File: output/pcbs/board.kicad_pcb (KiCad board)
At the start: 2 copper layers, 122.3 x 101.1 mm, 48 parts, among them J1 Jumper, J2 Jumper

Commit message: finish up
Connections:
- MCU1 pad 25: B- -> Bminus
- MCU2 pad 25: B- -> Bminus
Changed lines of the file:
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@@
 (net 39 "P8")
 (net 40 "P9")
-(net 41 "B+")
-(net 42 "B-")
+(net 41 "Bplus")
+(net 42 "Bminus")
 (net 43 "Braw")
-(net 44 "Bminus")
-(net 45 "Bplus")
   (net_class Default "This is the default net class."
     (clearance 0.2)
@@
 (add_net "P8")
 (add_net "P9")
-(add_net "B+")
-(add_net "B-")
-(add_net "Braw")
-(add_net "Bminus")
-(add_net "Bplus")
   )
   (net_class Power "This is the power net class."
@@
 (add_net "GND")
 (add_net "VCC")
+(add_net "Bplus")
+(add_net "Bminus")
+(add_net "Braw")
   )
       (module PG1350 (layer F.Cu)
@@
           (fp_text user "B+" (at -16.51 -4.8 360) (layer B.SilkS) (effects (font (size 0.8 0.8) (thickness 0.15)) (justify mirror)))
           (fp_text user "B-" (at -16.51 4.8 360) (layer B.SilkS) (effects (font (size 0.8 0.8) (thickness 0.15)) (justify mirror)))
-          (pad 25 thru_hole roundrect (at -16.51 -7.62 0) (size 1.5 1.5) (drill 1.0922) (layers *.Cu *.SilkS *.Mask) (roundrect_rratio 0.25) (net 41 "B+"))
-          (pad 25 thru_hole roundrect (at -16.51 7.62 0) (size 1.5 1.5) (drill 1.0922) (layers *.Cu *.SilkS *.Mask) (roundrect_rratio 0.25) (net 42 "B-"))
+          (pad 25 thru_hole roundrect (at -16.51 -7.62 0) (size 1.5 1.5) (drill 1.0922) (layers *.Cu *.SilkS *.Mask) (roundrect_rratio 0.25) (net 41 "Bplus"))
+          (pad 25 thru_hole roundrect (at -16.51 7.62 0) (size 1.5 1.5) (drill 1.0922) (layers *.Cu *.SilkS *.Mask) (roundrect_rratio 0.25) (net 42 "Bminus"))
         )
         (module ProMicro (layer F.Cu)
@@
           (fp_text user "B+" (at -16.51 4.8 360) (layer F.SilkS) (effects (font (size 0.8 0.8) (thickness 0.15)) ))
           (fp_text user "B-" (at -16.51 -4.8 360) (layer F.SilkS) (effects (font (size 0.8 0.8) (thickness 0.15)) ))
-          (pad 25 thru_hole roundrect (at -16.51 7.62 0) (size 1.5 1.5) (drill 1.0922) (layers *.Cu *.SilkS *.Mask) (roundrect_rratio 0.25) (net 41 "B+"))
-          (pad 25 thru_hole roundrect (at -16.51 -7.62 0) (size 1.5 1.5) (drill 1.0922) (layers *.Cu *.SilkS *.Mask) (roundrect_rratio 0.25) (net 42 "B-"))
+          (pad 25 thru_hole roundrect (at -16.51 7.62 0) (size 1.5 1.5) (drill 1.0922) (layers *.Cu *.SilkS *.Mask) (roundrect_rratio 0.25) (net 41 "Bplus"))
+          (pad 25 thru_hole roundrect (at -16.51 -7.62 0) (size 1.5 1.5) (drill 1.0922) (layers *.Cu *.SilkS *.Mask) (roundrect_rratio 0.25) (net 42 "Bminus"))
         )
         (module SMDPad (layer F.Cu)
@@
             (fp_text reference "PAD2" (at 0 0) (layer F.SilkS) hide (effects (font (size 1.27 1.27) (thickness 0.15))))
             (fp_text value "" (at 0 0) (layer F.SilkS) hide (effects (font (size 1.27 1.27) (thickness 0.15))))
-            (pad 1 smd rect (at 0 0 0) (size 1.5 1.5) (layers F.Cu F.Paste F.Mask) (net 44 "Bminus"))
+            (pad 1 smd rect (at 0 0 0) (size 1.5 1.5) (layers F.Cu F.Paste F.Mask) (net 42 "Bminus"))
 (fp_text user B- (at -2.25 0 0) (layer F.SilkS) (effects (font (size 0.8 0.8) (thickness 0.15)) ))
-            (pad 1 smd rect (at 0 0 0) (size 1.5 1.5) (layers B.Cu B.Paste B.Mask) (net 44 "Bminus"))
+            (pad 1 smd rect (at 0 0 0) (size 1.5 1.5) (layers B.Cu B.Paste B.Mask) (net 42 "Bminus"))
 (fp_text user B- (at -2.25 0 0) (layer B.SilkS) (effects (font (size 0.8 0.8) (thickness 0.15)) (justify mirror)))
         )
@@
         (clearance 0.1905) (net 43 "Braw"))
         (pad 2 smd rect (at 0.50038 0 270) (size 0.635 1.143) (layers B.Cu B.Paste B.Mask)
-        (clearance 0.1905) (net 45 "Bplus")))
+        (clearance 0.1905) (net 41 "Bplus")))
         (module lib:Jumper (layer F.Cu)
         (at 113.5 -10.2 270)
@@
         (clearance 0.1905) (net 43 "Braw"))
         (pad 2 smd rect (at 0.50038 0 270) (size 0.635 1.143) (layers F.Cu F.Paste F.Mask)
-        (clearance 0.1905) (net 45 "Bplus")))
+        (clearance 0.1905) (net 41 "Bplus")))
         (module E73:SPDT_C128955 (layer F.Cu)
             (at 120 -10.2 270)
@@
             (pad "" np_thru_hole circle (at -1.5 0) (size 1 1) (drill 0.9) (layers *.Cu *.Mask))
             (pad 1 smd rect (at 2.25 2.075 270) (size 0.9 1.25) (layers F.Cu F.Paste F.Mask) (net 43 "Braw"))
-            (pad 2 smd rect (at -0.75 2.075 270) (size 0.9 1.25) (layers F.Cu F.Paste F.Mask) (net 45 "Bplus"))
+            (pad 2 smd rect (at -0.75 2.075 270) (size 0.9 1.25) (layers F.Cu F.Paste F.Mask) (net 41 "Bplus"))
             (pad 3 smd rect (at -2.25 2.075 270) (size 0.9 1.25) (layers F.Cu F.Paste F.Mask))
             (pad "" smd rect (at 3.7 -1.1 270) (size 0.9 0.9) (layers F.Cu F.Paste F.Mask))
@@
             (pad "" np_thru_hole circle (at -1.5 0) (size 1 1) (drill 0.9) (layers *.Cu *.Mask))
             (pad 1 smd rect (at -2.25 2.075 270) (size 0.9 1.25) (layers B.Cu B.Paste B.Mask) (net 43 "Braw"))
-            (pad 2 smd rect (at 0.75 2.075 270) (size 0.9 1.25) (layers B.Cu B.Paste B.Mask) (net 45 "Bplus"))
+            (pad 2 smd rect (at 0.75 2.075 270) (size 0.9 1.25) (layers B.Cu B.Paste B.Mask) (net 41 "Bplus"))
             (pad 3 smd rect (at 2.25 2.075 270) (size 0.9 1.25) (layers B.Cu B.Paste B.Mask))
             (pad "" smd rect (at 3.7 -1.1 270) (size 0.9 0.9) (layers B.Cu B.Paste B.Mask))

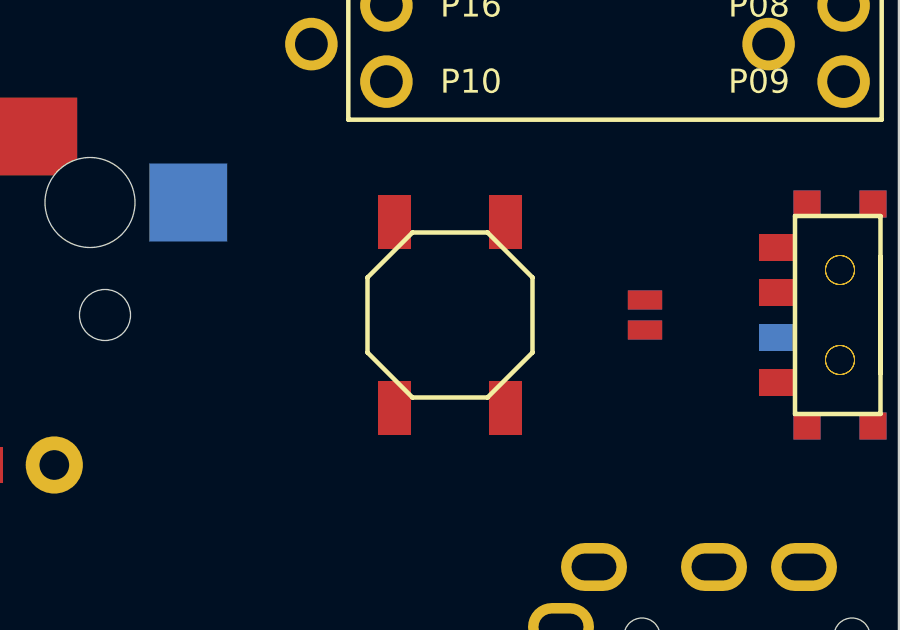
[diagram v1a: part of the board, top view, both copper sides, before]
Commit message: Use a better reset button footprint (#6)
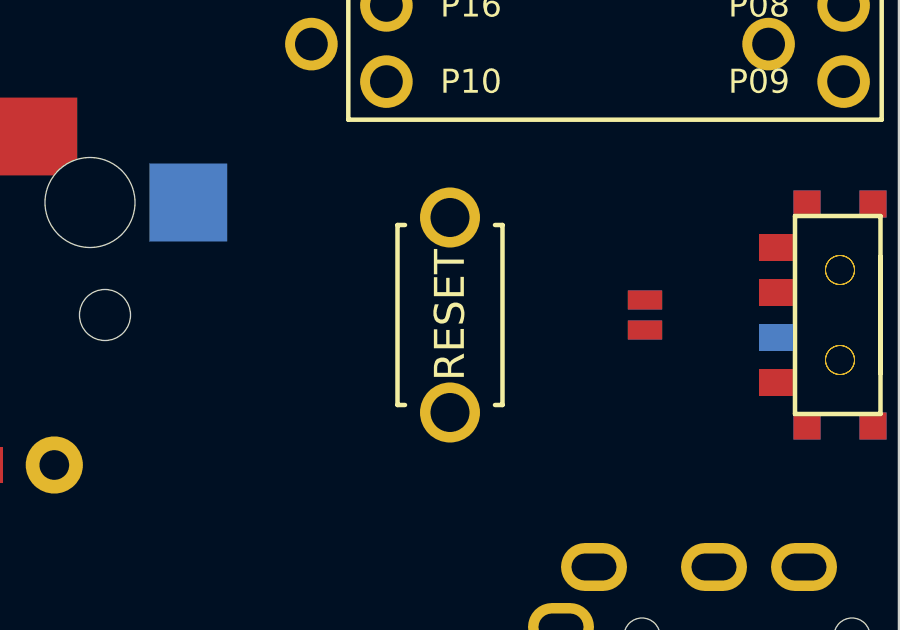
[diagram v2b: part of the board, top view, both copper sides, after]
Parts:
- removed B2: , E73:SW_TACT_ALPS_SKQGABE010
- B1: footprint E73:SW_TACT_ALPS_SKQGABE010 -> kbd:ResetSW
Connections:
- B1 pad 1: GND -> RST
- B1 pad 2: RST -> GND
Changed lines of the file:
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@@
             (pad "" smd rect (at -3.7 -1.1 270) (size 0.9 0.9) (layers B.Cu B.Paste B.Mask))
         )
-    (module E73:SW_TACT_ALPS_SKQGABE010 (layer F.Cu)
-        (descr "Low-profile SMD Tactile Switch, https://www.e-switch.com/product-catalog/tact/product-lines/tl3342-series-low-profile-smt-tact-switch")
-        (tags "SPST Tactile Switch")
-        (at 107 -10.2 270)
-        (fp_text reference "B1" (at 0 0) (layer F.SilkS) hide (effects (font (size 1.27 1.27) (thickness 0.15))))
-        (fp_text value "" (at 0 0) (layer F.SilkS) hide (effects (font (size 1.27 1.27) (thickness 0.15))))
-        (fp_line (start 2.75 1.25) (end 1.25 2.75) (layer F.SilkS) (width 0.15))
-        (fp_line (start 2.75 -1.25) (end 1.25 -2.75) (layer F.SilkS) (width 0.15))
-        (fp_line (start 2.75 -1.25) (end 2.75 1.25) (layer F.SilkS) (width 0.15))
-        (fp_line (start -1.25 2.75) (end 1.25 2.75) (layer F.SilkS) (width 0.15))
-        (fp_line (start -1.25 -2.75) (end 1.25 -2.75) (layer F.SilkS) (width 0.15))
-        (fp_line (start -2.75 1.25) (end -1.25 2.75) (layer F.SilkS) (width 0.15))
-        (fp_line (start -2.75 -1.25) (end -1.25 -2.75) (layer F.SilkS) (width 0.15))
-        (fp_line (start -2.75 -1.25) (end -2.75 1.25) (layer F.SilkS) (width 0.15))
-        (pad 1 smd rect (at -3.1 -1.85 270) (size 1.8 1.1) (layers F.Cu F.Paste F.Mask) (net 29 "GND"))
-        (pad 1 smd rect (at 3.1 -1.85 270) (size 1.8 1.1) (layers F.Cu F.Paste F.Mask) (net 29 "GND"))
-        (pad 2 smd rect (at -3.1 1.85 270) (size 1.8 1.1) (layers F.Cu F.Paste F.Mask) (net 30 "RST"))
-        (pad 2 smd rect (at 3.1 1.85 270) (size 1.8 1.1) (layers F.Cu F.Paste F.Mask) (net 30 "RST"))
-    )
-    (module E73:SW_TACT_ALPS_SKQGABE010 (layer F.Cu)
-        (descr "Low-profile SMD Tactile Switch, https://www.e-switch.com/product-catalog/tact/product-lines/tl3342-series-low-profile-smt-tact-switch")
-        (tags "SPST Tactile Switch")
-        (at 107 -10.2 270)
-        (fp_text reference "B2" (at 0 0) (layer F.SilkS) hide (effects (font (size 1.27 1.27) (thickness 0.15))))
-        (fp_text value "" (at 0 0) (layer F.SilkS) hide (effects (font (size 1.27 1.27) (thickness 0.15))))
-        (fp_line (start 2.75 1.25) (end 1.25 2.75) (layer B.SilkS) (width 0.15))
-        (fp_line (start 2.75 -1.25) (end 1.25 -2.75) (layer B.SilkS) (width 0.15))
-        (fp_line (start 2.75 -1.25) (end 2.75 1.25) (layer B.SilkS) (width 0.15))
-        (fp_line (start -1.25 2.75) (end 1.25 2.75) (layer B.SilkS) (width 0.15))
-        (fp_line (start -1.25 -2.75) (end 1.25 -2.75) (layer B.SilkS) (width 0.15))
-        (fp_line (start -2.75 1.25) (end -1.25 2.75) (layer B.SilkS) (width 0.15))
-        (fp_line (start -2.75 -1.25) (end -1.25 -2.75) (layer B.SilkS) (width 0.15))
-        (fp_line (start -2.75 -1.25) (end -2.75 1.25) (layer B.SilkS) (width 0.15))
-        (pad 1 smd rect (at -3.1 -1.85 270) (size 1.8 1.1) (layers B.Cu B.Paste B.Mask) (net 29 "GND"))
-        (pad 1 smd rect (at 3.1 -1.85 270) (size 1.8 1.1) (layers B.Cu B.Paste B.Mask) (net 29 "GND"))
-        (pad 2 smd rect (at -3.1 1.85 270) (size 1.8 1.1) (layers B.Cu B.Paste B.Mask) (net 30 "RST"))
-        (pad 2 smd rect (at 3.1 1.85 270) (size 1.8 1.1) (layers B.Cu B.Paste B.Mask) (net 30 "RST"))
-    )
+            (module kbd:ResetSW (layer F.Cu)
+                (descr "Two pin through hole Tactile Switch, the same as on the Corne")
+                (tags "Tactile Switch")
+                (at 107 -10.2 270)
+                (fp_text reference "B1" (at 0 2.55) (layer F.SilkS) hide (effects (font (size 1 1) (thickness 0.15))))
+                (fp_text value "" (at 0 -2.55) (layer F.Fab) (effects (font (size 1 1) (thickness 0.15))))
+                (fp_text user RESET (at 0 0 270) (layer F.SilkS) (effects (font (size 1 1) (thickness 0.15))))
+                (fp_text user RESET (at 0.127 0 270) (layer B.SilkS) (effects (font (size 1 1) (thickness 0.15)) (justify mirror)))
+                (fp_line (start 3 1.5) (end 3 1.75) (layer B.SilkS) (width 0.15))
+                (fp_line (start 3 1.75) (end -3 1.75) (layer B.SilkS) (width 0.15))
+                (fp_line (start -3 1.75) (end -3 1.5) (layer B.SilkS) (width 0.15))
+                (fp_line (start -3 -1.5) (end -3 -1.75) (layer B.SilkS) (width 0.15))
+                (fp_line (start -3 -1.75) (end 3 -1.75) (layer B.SilkS) (width 0.15))
+                (fp_line (start 3 -1.75) (end 3 -1.5) (layer B.SilkS) (width 0.15))
+                (fp_line (start -3 1.75) (end 3 1.75) (layer F.SilkS) (width 0.15))
+                (fp_line (start 3 1.75) (end 3 1.5) (layer F.SilkS) (width 0.15))
+                (fp_line (start -3 1.75) (end -3 1.5) (layer F.SilkS) (width 0.15))
+                (fp_line (start -3 -1.75) (end -3 -1.5) (layer F.SilkS) (width 0.15))
+                (fp_line (start -3 -1.75) (end 3 -1.75) (layer F.SilkS) (width 0.15))
+                (fp_line (start 3 -1.75) (end 3 -1.5) (layer F.SilkS) (width 0.15))
+                (pad 2 thru_hole circle (at -3.25 0 270) (size 2 2) (drill 1.3) (layers *.Cu *.Mask F.SilkS) (net 29 "GND"))
+                (pad 1 thru_hole circle (at 3.25 0 270) (size 2 2) (drill 1.3) (layers *.Cu *.Mask F.SilkS) (net 30 "RST"))
+            )
             (gr_text "samoklava v0.1\nby soundmonster" (at 31.5 0 0) (layer F.SilkS)
                 (effects (font (size 1 1) (thickness 0.15)) (justify left))
